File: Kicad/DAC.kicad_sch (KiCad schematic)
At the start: 23 parts, among them U4 PCM5242RHBR

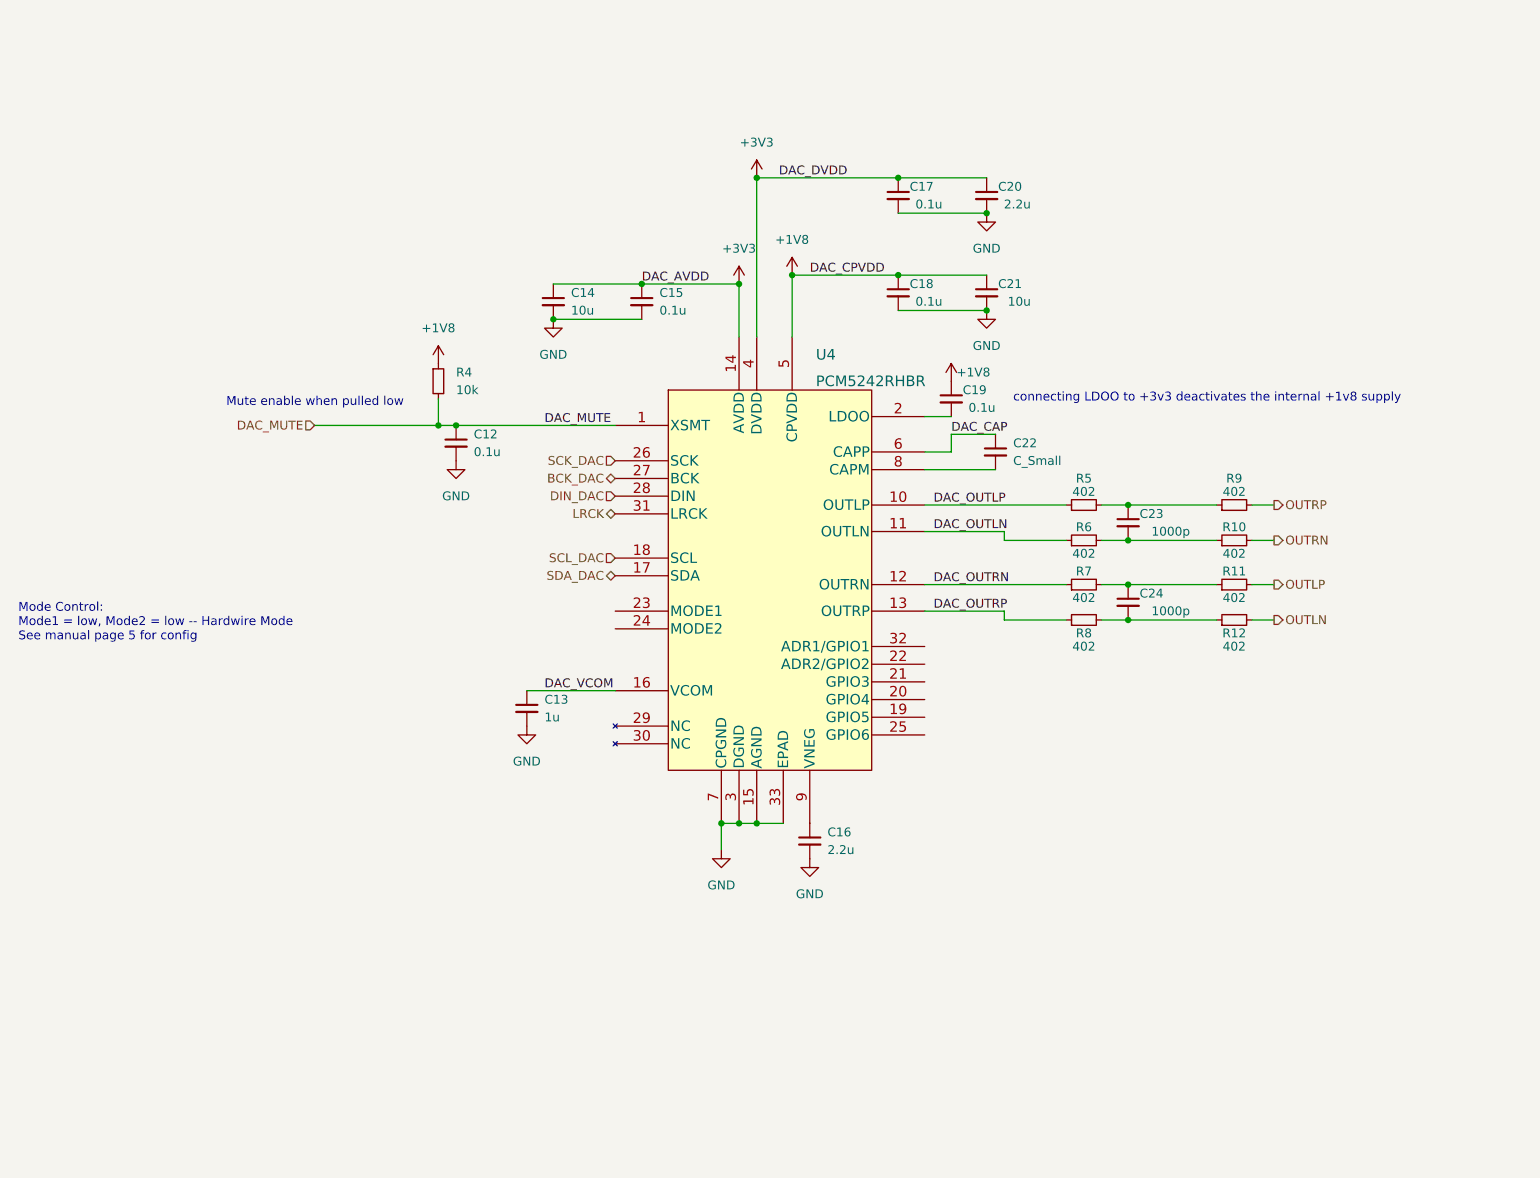
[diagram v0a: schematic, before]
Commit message: changed dac to ES9033
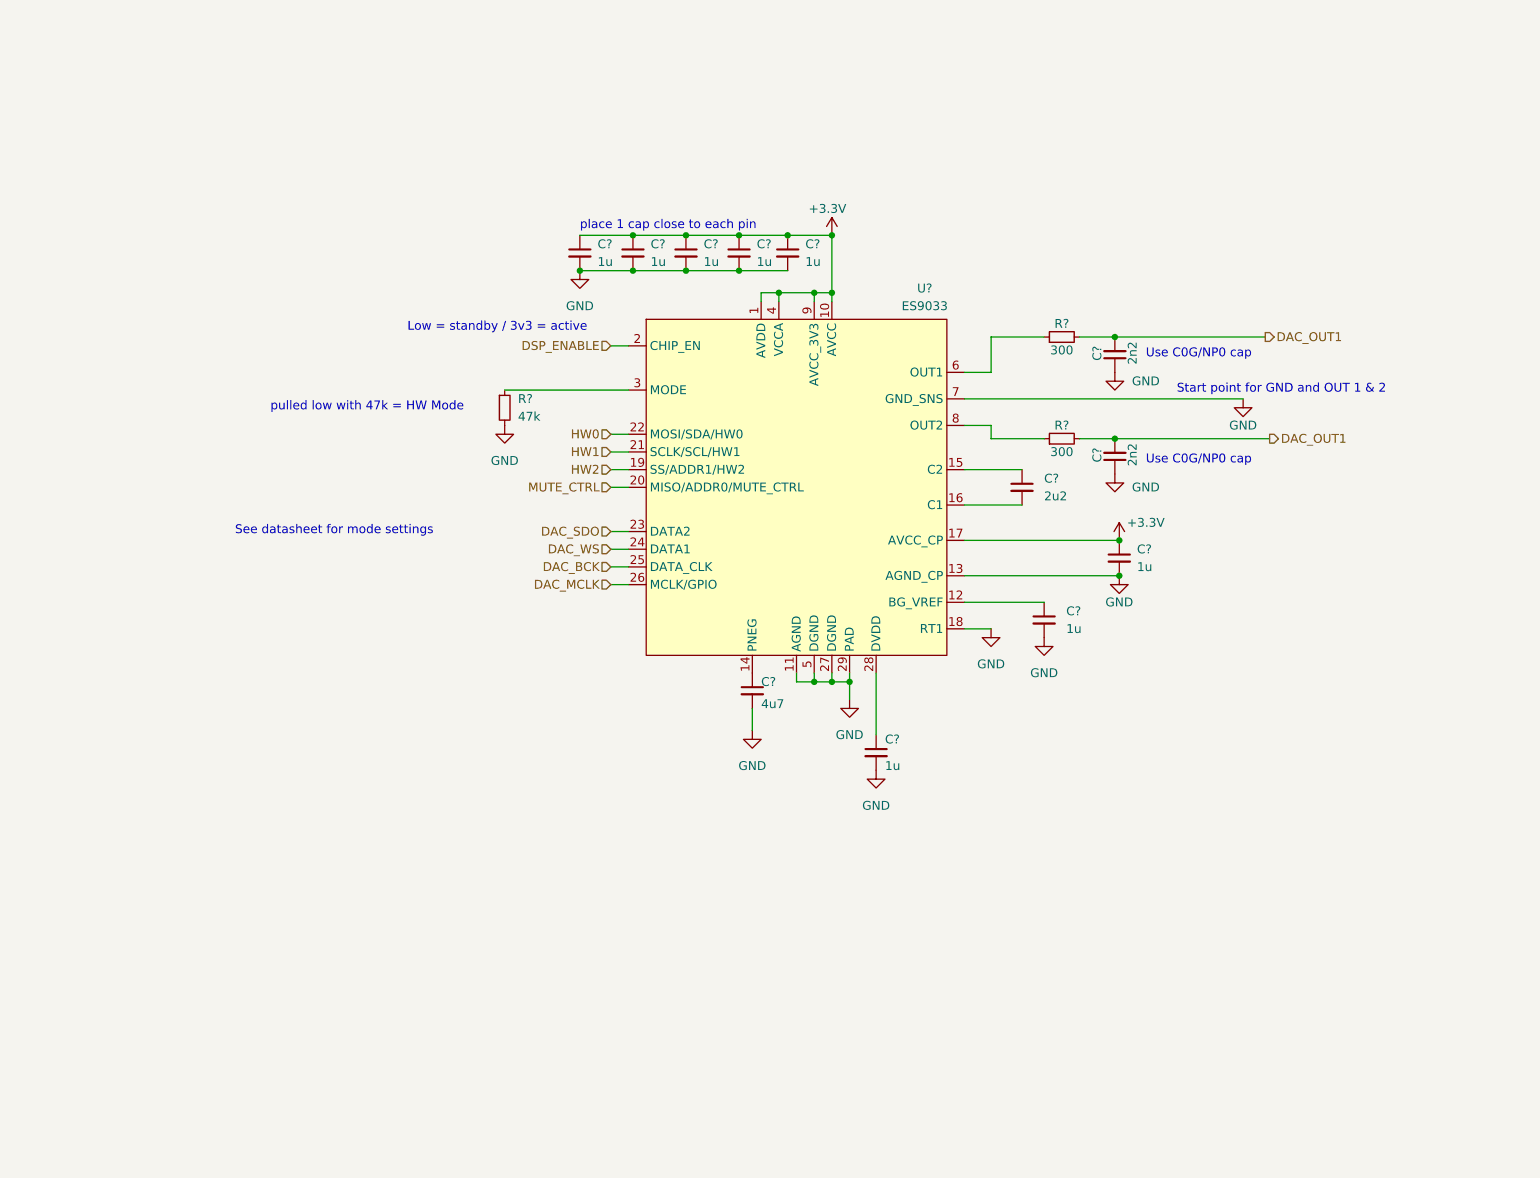
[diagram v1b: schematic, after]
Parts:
- removed C12, C15, C17, C18, C19: 0.1u, Capacitor_SMD:C_0805_2012Metric, symbol Device:C_Small
- removed C13: 1u, Capacitor_SMD:C_0805_2012Metric, symbol Device:C_Small
- removed C14, C21: 10u, Capacitor_SMD:C_0805_2012Metric, symbol Device:C_Small
- removed C16, C20: 2.2u, Capacitor_SMD:C_0805_2012Metric, symbol Device:C_Small
- removed C22: C_Small, Capacitor_SMD:C_0805_2012Metric, symbol Device:C_Small
- removed C23, C24: 1000p, Capacitor_SMD:C_0805_2012Metric, symbol Device:C_Small
- removed R10, R11, R12, R5, R6, R7, R8, R9: 402, Resistor_SMD:R_0805_2012Metric, symbol Device:R_Small
- removed R4: 10k, symbol Device:R_Small
- removed U4: PCM5242RHBR, project_footprints:PCM5242RHBR, symbol project_sym_lib:PCM5242RHBR
- added C? (x8): 1u, symbol Device:C_Small
- added C?: 4u7, symbol Device:C_Small
- added C?: 2u2, symbol Device:C_Small
- added C? (x2): 2n2, symbol Device:C_Small
- added R?: 47k, symbol Device:R_Small
- added R? (x2): 300, symbol Device:R_Small
- added U?: ES9033, symbol project_sym_lib:ES9033
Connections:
- net GND: now also C?.1, C?.1, C?.2, C?.2, C?.2, C?.2, C?.2, C?.2, C?.2, C?.2, C?.2, R?.2, U?.11 (AGND), U?.13 (AGND_CP), U?.18 (RT1), U?.27 (DGND), U?.29 (PAD), U?.5 (DGND), U?.7 (GND_SNS)
- new net: R?.1, U?.3 (MODE)
- new net: C?.1, U?.12 (BG_VREF)
- new net: C?.1, U?.14 (PNEG)
- new net: C?.1, U?.15 (C2)
- new net: C?.2, U?.16 (C1)
- new net: C?.1, U?.28 (DVDD)
- new net: R?.1, U?.6 (OUT1)
- new net: R?.1, U?.8 (OUT2)
- new net +3.3V: C?.1, C?.1, C?.1, C?.1, C?.1, C?.1, U?.1 (AVDD), U?.10 (AVCC), U?.17 (AVCC_CP), U?.4 (VCCA), U?.9 (AVCC_3V3)
- new net DAC_BCK: U?.25 (DATA_CLK)
- new net DAC_MCLK: U?.26 (MCLK/GPIO)
- new net DAC_OUT1: C?.2, C?.2, R?.2, R?.2
- new net DAC_SDO: U?.23 (DATA2)
- new net DAC_WS: U?.24 (DATA1)
- new net DSP_ENABLE: U?.2 (CHIP_EN)
- new net HW0: U?.22 (MOSI/SDA/HW0)
- new net HW1: U?.21 (SCLK/SCL/HW1)
- new net HW2: U?.19 (SS/ADDR1/HW2)
- new net MUTE_CTRL: U?.20 (MISO/ADDR0/MUTE_CTRL)
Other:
- note added: "Low = standby / 3v3 = active"
- note added: "See datasheet for mode settings"
- note added: "Start point for GND and OUT 1 & 2"
- note added: "Use C0G/NP0 cap"
- note added: "place 1 cap close to each pin"
- note added: "pulled low with 47k = HW Mode"
- note removed: "Mode Control: Mode1 = low, Mode2 = low -- Hardwire Mode See manual page 5 for config"
- note removed: "Mute enable when pulled low"
- note removed: "connecting LDOO to +3v3 deactivates the internal +1v8 supply"

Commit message: updated DAC circut
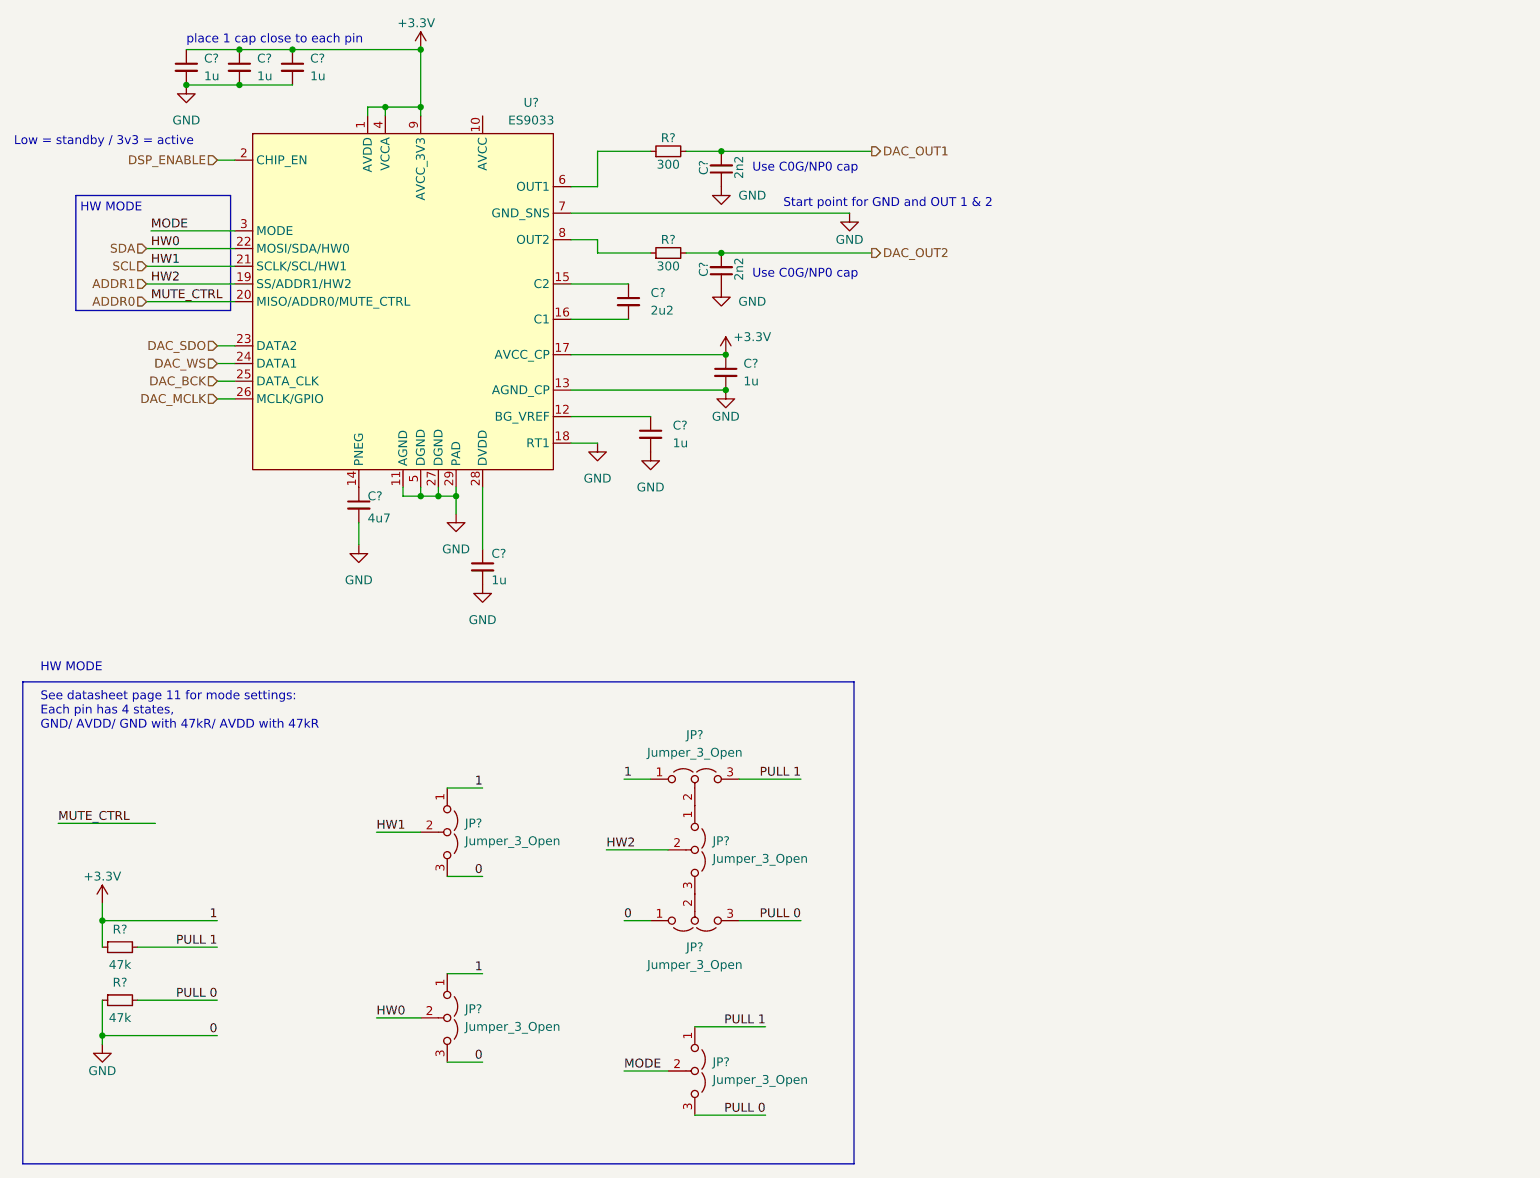
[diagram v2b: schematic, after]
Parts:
- removed C? (x2): 1u, symbol Device:C_Small
- removed R?: 47k, symbol Device:R_Small
- added JP? (x6): Jumper_3_Open, symbol Jumper:Jumper_3_Open
- added R? (x2): 47k, symbol Device:R_Small
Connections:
- net +3.3V: now also JP?.1 (A), JP?.1 (A), JP?.1 (A), R?.1; no longer U?.10 (AVCC)
- net DAC_OUT1: no longer C?.2, R?.2
- net GND: now also JP?.1 (A), JP?.3 (B), JP?.3 (B), R?.1
- net MODE: now reaches U?.3 (MODE)
- net MODE: now also JP?.2 (C)
- net HW0 renamed SDA
- net SDA: now also JP?.2 (C)
- net HW1 renamed SCL
- net SCL: now also JP?.2 (C)
- net HW2 renamed ADDR1
- net ADDR1: now also JP?.2 (C)
- net MUTE_CTRL renamed ADDR0
- new net: JP?.1 (A), JP?.2 (C)
- new net: JP?.2 (C), JP?.3 (B)
- new net DAC_OUT2: C?.2, R?.2
- new net PULL 0: JP?.3 (B), JP?.3 (B), R?.2
- new net PULL 1: JP?.1 (A), JP?.3 (B), R?.2
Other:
- note added: "HW MODE"
- note added: "See datasheet page 11 for mode settings: Each pin has 4 states, GND/ AVDD/ GND with 47kR/ AVDD with 47kR"
- note removed: "See datasheet for mode settings"
- note removed: "pulled low with 47k = HW Mode"
- moved on the sheet: C?, R?, U?

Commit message: updated footprints, basic pcb laypout
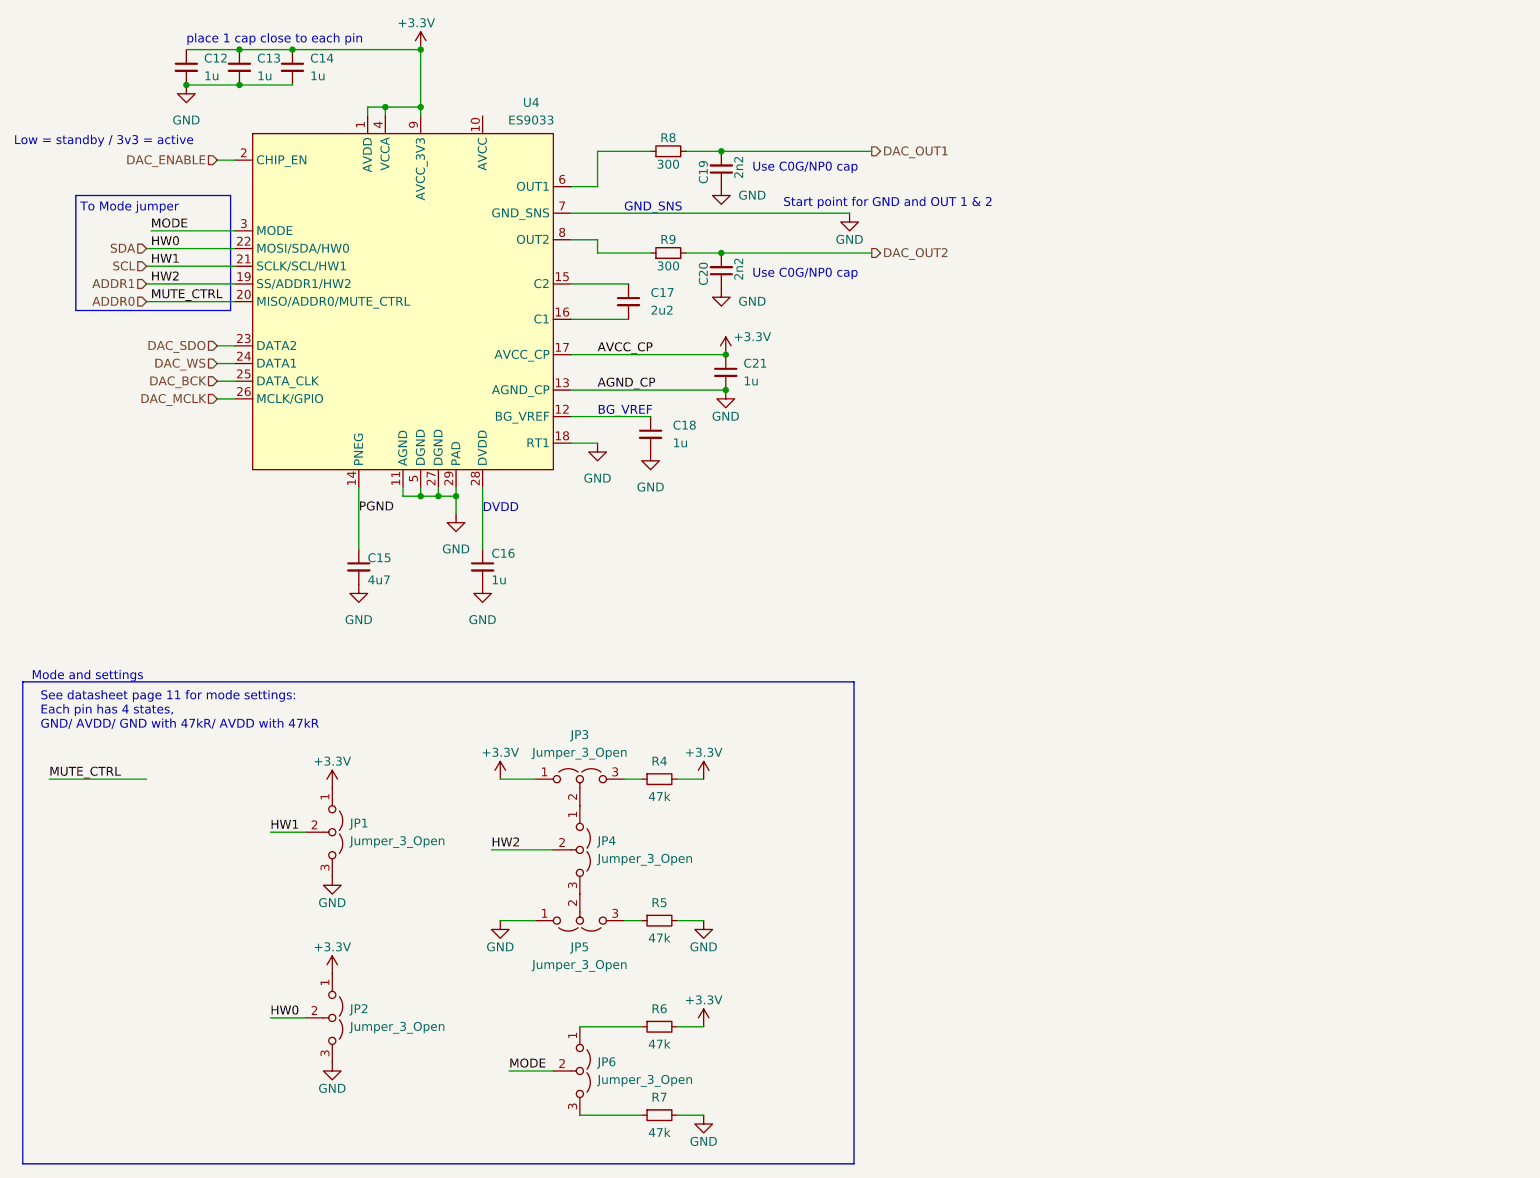
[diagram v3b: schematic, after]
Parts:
- removed R? (x2): 47k, symbol Device:R_Small
- added R4, R5, R6, R7: 47k, Resistor_SMD:R_0805_2012Metric, symbol Device:R_Small
- C12, C13, C14, C15, C18, C19, C20, C21: renamed from C?; footprint (none) -> Capacitor_SMD:C_0805_2012Metric
- JP1, JP2, JP3, JP4, JP5, JP6: renamed from JP?; footprint (none) -> Connector_PinHeader_2.54mm:PinHeader_1x03_P2.54mm_Vertical
- R8, R9: renamed from R?; footprint (none) -> Resistor_SMD:R_0805_2012Metric
- U4: renamed from U?; footprint (none) -> Package_DFN_QFN:QFN-28-1EP_5x5mm_P0.5mm_EP3.35x3.35mm_ThermalVias
- gave numbers to parts that had none: 2
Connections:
- net +3.3V: now also R4.2, R6.2
- net GND: now also R5.2, R7.2
- net PGND: now reaches C15.1, U4.14 (PNEG)
- net DSP_ENABLE renamed DAC_ENABLE
- net PULL 0: no longer names the net of JP5.3 (B)
- net PULL 0: now also R5.1; no longer JP6.3 (B)
- net PULL 1: no longer names the net of JP3.3 (B)
- net PULL 1: now also R4.1; no longer JP6.1 (A)
- new net: JP6.1 (A), R6.1
- new net: JP6.3 (B), R7.1
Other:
- note added: "BG_VREF"
- note added: "DVDD"
- note added: "GND_SNS"
- note added: "Mode and settings"
- note added: "To Mode jumper"
- note removed: "HW MODE"
- moved on the sheet: C15, JP1, JP2, JP3, JP4, JP5, JP6
